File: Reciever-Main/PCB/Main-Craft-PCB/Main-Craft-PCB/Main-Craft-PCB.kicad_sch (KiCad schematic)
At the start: 17 parts

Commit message: Continue PCB work
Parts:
- added D? (x2): IR_Sender_?, symbol Device:LED
- added J? (x2): IR_Receiver_?, symbol Connector:Conn_01x03_Male
- added Q? (x2): 2N2219, Package_TO_SOT_THT:TO-39-3, symbol Transistor_BJT:2N2219
- added R? (x6): 10K, symbol Device:R
- added R? (x2): 4K7, symbol Device:R
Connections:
- net +5V: now also D?.2 (A), D?.2 (A), J?.3 (Pin_3), J?.3 (Pin_3), R?.1, R?.1
- net GND: now also J?.1 (Pin_1), J?.1 (Pin_1), Q?.1 (E), Q?.1 (E)
- net at D?.1 (K): now also R?.1; no longer Q?.3 (C) (x2)
- net ESC_? renamed BUZZER
- new net: D?.1 (K), R?.1 (x2)
- new net: Q?.3 (C), R?.2 (x4)
- new net: J?.2 (Pin_2), R?.2 (x2)
- new net: Q?.2 (B), R?.2 (x2)
- new net IR_?_OUT: R?.1, R?.1
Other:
- moved on the sheet: D?, Q?, R?

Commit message: Add components to the Schematic
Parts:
- added C? (x5): 100nF, symbol Device:C
- added D? (x2): 1N5817, Diode_THT:D_DO-41_SOD81_P10.16mm_Horizontal, symbol Diode:1N5817
- added SW?: SW_SPDT, symbol Switch:SW_SPDT
- added U?: LM2940-5.0, symbol Regulator_Linear:LM1117-3.3
- added U?: LM2940-3.0, symbol Regulator_Linear:LM1117-3.3
- J?: value Conn_02x04_Odd_Even -> nRF24L01_Conn
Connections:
- net +5V: now also U?.18 (+5V), C?.2, U?.2 (VO)
- net Earth: now reaches J?.1 (Pin_1)
- net Earth: now also C?.1, C?.1, C?.1, C?.1, C?.1, D?.2 (A), D?.2 (A), U?.1 (GND), U?.1 (GND)
- net +3V3: now reaches J?.2 (Pin_2)
- net +3V3: now also U?.16 (+3V3), C?.2, C?.2, U?.2 (VO)
- net NRF_CE: now reaches J?.3 (Pin_3)
- net NRF_CSN: now reaches J?.4 (Pin_4)
- net NRF_SCK: now reaches J?.5 (Pin_5)
- net NRF_MOSI: now reaches J?.6 (Pin_6)
- net NRF_MISO: now reaches J?.7 (Pin_7)
- net NRF_IRQ: now reaches J?.8 (Pin_8)
- new net +BATT: SW?.1 (A)
- new net BAT_PWR: C?.2, C?.2, D?.1 (K), D?.1 (K), SW?.2 (B), U?.3 (VI), U?.3 (VI)
- no-connect marks 0 -> 8
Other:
- moved on the sheet: J?

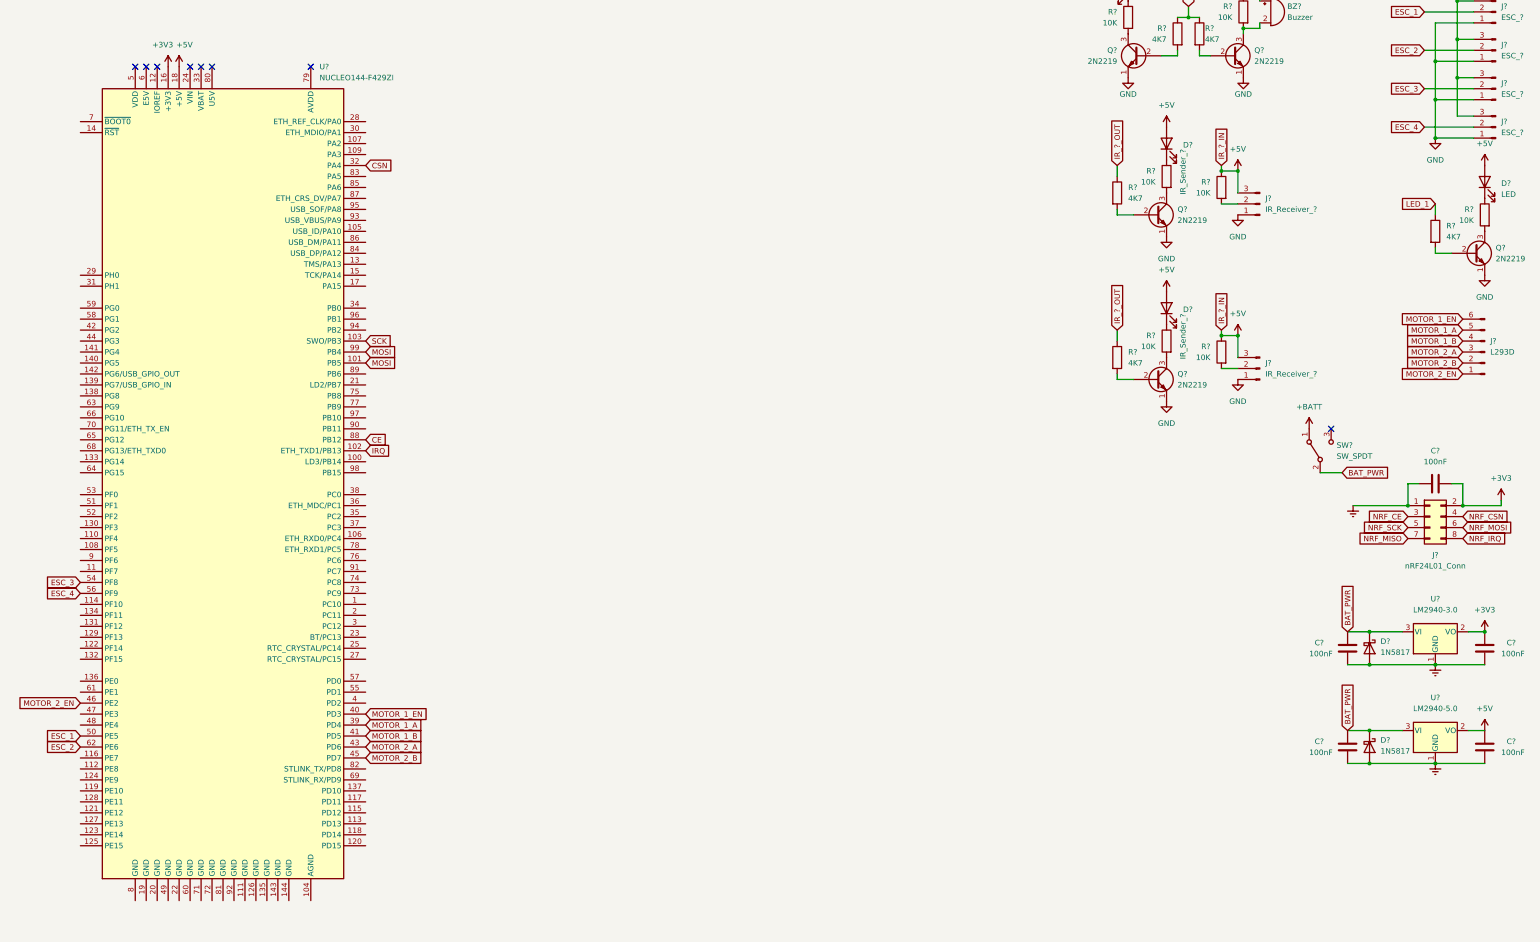
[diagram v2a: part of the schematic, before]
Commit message: Add Battery Comparitors to the Schematic
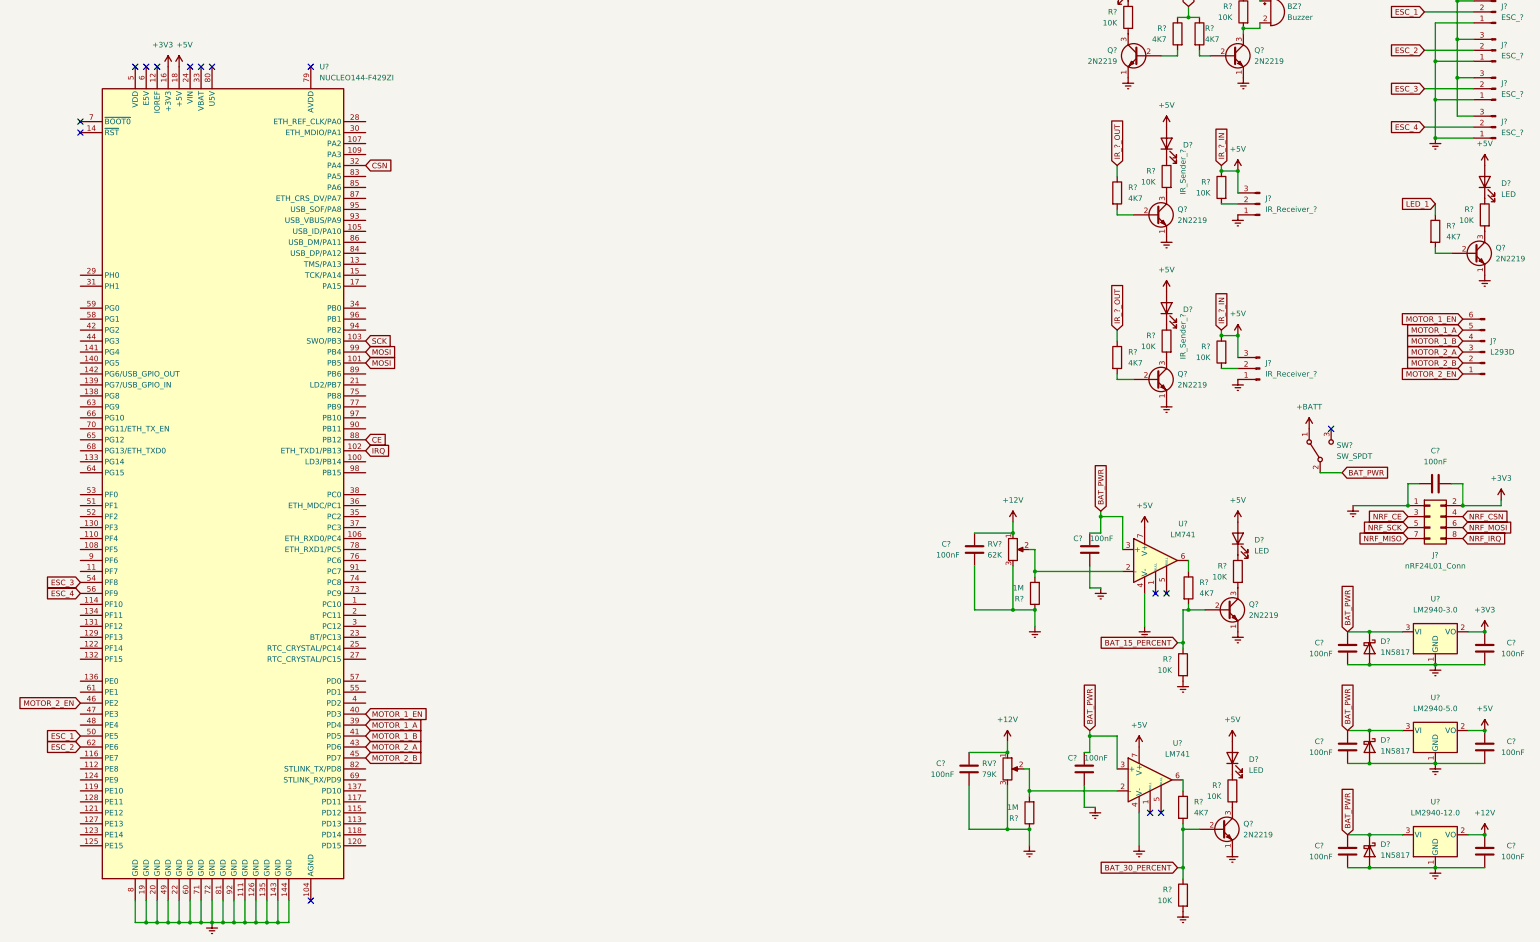
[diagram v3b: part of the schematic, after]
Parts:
- added C? (x4): 100nF, Capacitor_SMD:C_0603_1608Metric, symbol Device:C
- added C? (x2): 100nF, symbol Device:C
- added D? (x2): LED, symbol Device:LED
- added D?: 1N5817, Diode_THT:D_DO-41_SOD81_P10.16mm_Horizontal, symbol Diode:1N5817
- added Q? (x2): 2N2219, Package_TO_SOT_THT:TO-39-3, symbol Transistor_BJT:2N2219
- added R? (x2): 4K7, symbol Device:R
- added R? (x2): 1M, Resistor_SMD:R_0603_1608Metric, symbol Device:R
- added R? (x4): 10K, symbol Device:R
- added RV?: 79K, symbol Device:R_Potentiometer
- added RV?: 62K, symbol Device:R_Potentiometer
- added U? (x2): LM741, symbol Amplifier_Operational:LM741
- added U?: LM2940-12.0, symbol Regulator_Linear:LM1117-3.3
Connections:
- net GND is gone; now on net Earth: J?.1 (Pin_1), J?.1 (Pin_1), J?.1 (Pin_1), J?.1 (Pin_1), J?.1 (Pin_1), J?.1 (Pin_1), Q?.1 (E), Q?.1 (E), Q?.1 (E), Q?.1 (E), Q?.1 (E)
- net +5V: now also D?.2 (A), D?.2 (A), U?.7 (V+), U?.7 (V+)
- net BAT_PWR: now also C?.1, C?.1, C?.2, D?.1 (K), U?.3 (+), U?.3 (+), U?.3 (VI)
- net Earth: now also U?.111 (GND), U?.126 (GND), U?.135 (GND), U?.143 (GND), U?.144 (GND), U?.19 (GND), U?.20 (GND), U?.22 (GND), U?.49 (GND), U?.60 (GND), U?.71 (GND), U?.72 (GND), U?.8 (GND), U?.81 (GND), U?.92 (GND), C?.1, C?.1, C?.2, C?.2, C?.2, C?.2, D?.2 (A), Q?.1 (E), Q?.1 (E), R?.1, R?.1, R?.2, R?.2, RV?.3, RV?.3, U?.1 (GND), U?.4 (V-), U?.4 (V-)
- new net: R?.1, U?.6 (x2)
- new net: D?.1 (K), R?.1 (x2)
- new net: R?.2, RV?.2, U?.2 (-) (x2)
- new net: Q?.3 (C), R?.2 (x2)
- new net +12V: C?.1, C?.1, C?.2, RV?.1, RV?.1, U?.2 (VO)
- new net BAT_15_PERCENT: Q?.2 (B), R?.1, R?.2
- new net BAT_30_PERCENT: Q?.2 (B), R?.1, R?.2
- no-connect marks 8 -> 15

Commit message: Update PCB
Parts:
- added BT?: Battery, symbol Device:Battery
- added F?: Fuse, symbol Device:Fuse
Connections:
- net +BATT: now also C?.1, C?.1, C?.2, C?.2, C?.2, D?.1 (K), D?.1 (K), D?.1 (K), U?.3 (+), U?.3 (+), U?.3 (VI), U?.3 (VI), U?.3 (VI)
- net Earth: now also BT?.2 (-)
- removed net BAT_PWR: C?.1, C?.1, C?.2, C?.2, C?.2, D?.1 (K), D?.1 (K), D?.1 (K), SW?.2 (B), U?.3 (+), U?.3 (+), U?.3 (VI), U?.3 (VI), U?.3 (VI)
- new net: F?.1, SW?.2 (B)
- new net: BT?.1 (+), F?.2
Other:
- moved on the sheet: SW?

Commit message: Change library names, update PCB to add IR sensors LEDs and Switches
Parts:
- removed D? (x2): IR_Sender_?, symbol Device:LED
- removed J? (x2): IR_Receiver_?, symbol Connector:Conn_01x03_Male
- removed Q? (x2): 2N2219, Package_TO_SOT_THT:TO-39-3, symbol Transistor_BJT:2N2219
- removed R? (x4): 10K, symbol Device:R
- removed R? (x2): 4K7, symbol Device:R
- added D? (x12): LED, symbol Device:LED
- added J? (x4): IR_SENSOR_?, symbol Connector:Conn_01x03_Male
- added Q? (x9): 2N2219, Package_TO_SOT_THT:TO-39-3, symbol Transistor_BJT:2N2219
- added R? (x9): 4K7, symbol Device:R
- added R? (x23): 10K, symbol Device:R
- added R? (x11): 1K, symbol Device:R
- added SW? (x4): SW_SPDT, symbol Switch:SW_SPDT
- added SW? (x5): SW_Push, symbol Switch:SW_Push
- J?: value L293D -> L298N
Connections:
- net +12V: now also D?.2 (A)
- net +3V3: now also D?.2 (A)
- net +5V: now also D?.2 (A), D?.2 (A), D?.2 (A), D?.2 (A), D?.2 (A), D?.2 (A), D?.2 (A), D?.2 (A), D?.2 (A), D?.2 (A), J?.3 (Pin_3), J?.3 (Pin_3), J?.3 (Pin_3), J?.3 (Pin_3), SW?.2, SW?.2, SW?.2, SW?.2, SW?.2, SW?.2 (B), SW?.2 (B), SW?.2 (B), SW?.2 (B)
- net Earth: now also J?.1 (Pin_1), J?.1 (Pin_1), J?.1 (Pin_1), J?.1 (Pin_1), Q?.1 (E), Q?.1 (E), Q?.1 (E), Q?.1 (E), Q?.1 (E), Q?.1 (E), Q?.1 (E), Q?.1 (E), Q?.1 (E), R?.2, R?.2, R?.2, R?.2, R?.2, R?.2, R?.2, R?.2, R?.2, R?.2, R?.2, R?.2, R?.2, R?.2
- new net: Q?.2 (B), R?.2 (x9)
- new net: D?.1 (K), R?.1 (x12)
- new net: Q?.3 (C), R?.2 (x9)
- new net: R?.1, R?.1, SW?.3 (C) (x4)
- new net: R?.1, R?.1, SW?.1 (x5)
- new net: R?.1, R?.1, SW?.1 (A) (x2)
- new net IR_1: J?.2 (Pin_2)
- new net IR_2: J?.2 (Pin_2)
- new net IR_3: J?.2 (Pin_2)
- new net IR_4: J?.2 (Pin_2)
- new net LED_10: R?.1
- new net LED_2: R?.1
- new net LED_3: R?.1
- new net LED_4: R?.1
- new net LED_5: R?.1
- new net LED_6: R?.1
- new net LED_7: R?.1
- new net LED_8: R?.1
- new net LED_9: R?.1
- new net SW_1: R?.2
- new net SW_10: R?.2
- new net SW_11: R?.2
- new net SW_12: R?.2
- new net SW_13: R?.2
- new net SW_2: R?.2
- new net SW_3: R?.2
- new net SW_4: R?.2
- new net SW_5: R?.2
- new net SW_6: R?.2
- new net SW_7: R?.2
- no-connect marks 15 -> 17
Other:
- moved on the sheet: BT?, BZ?, C?, D?, F?, J?, Q?, R?, RV?, SW?, U?

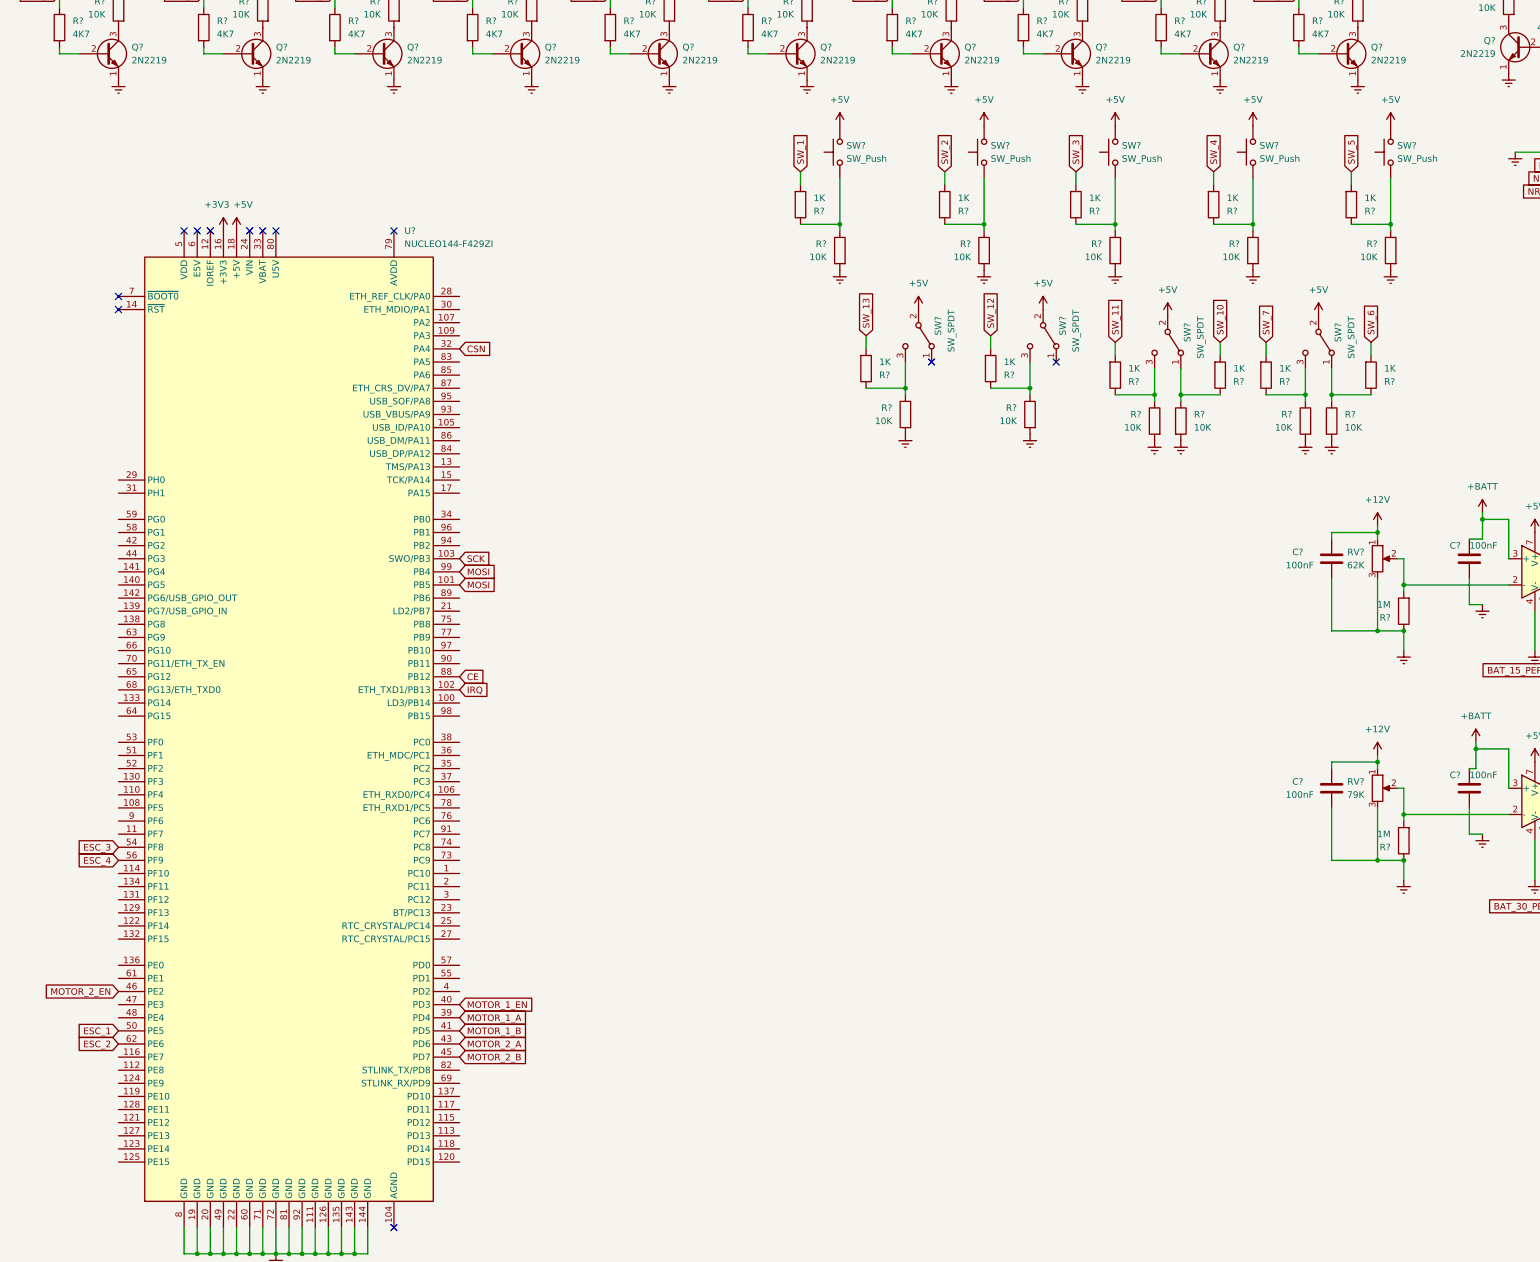
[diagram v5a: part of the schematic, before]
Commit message: Finish Pin mapping for PCB, update HARDWARE.h with updated pinmap
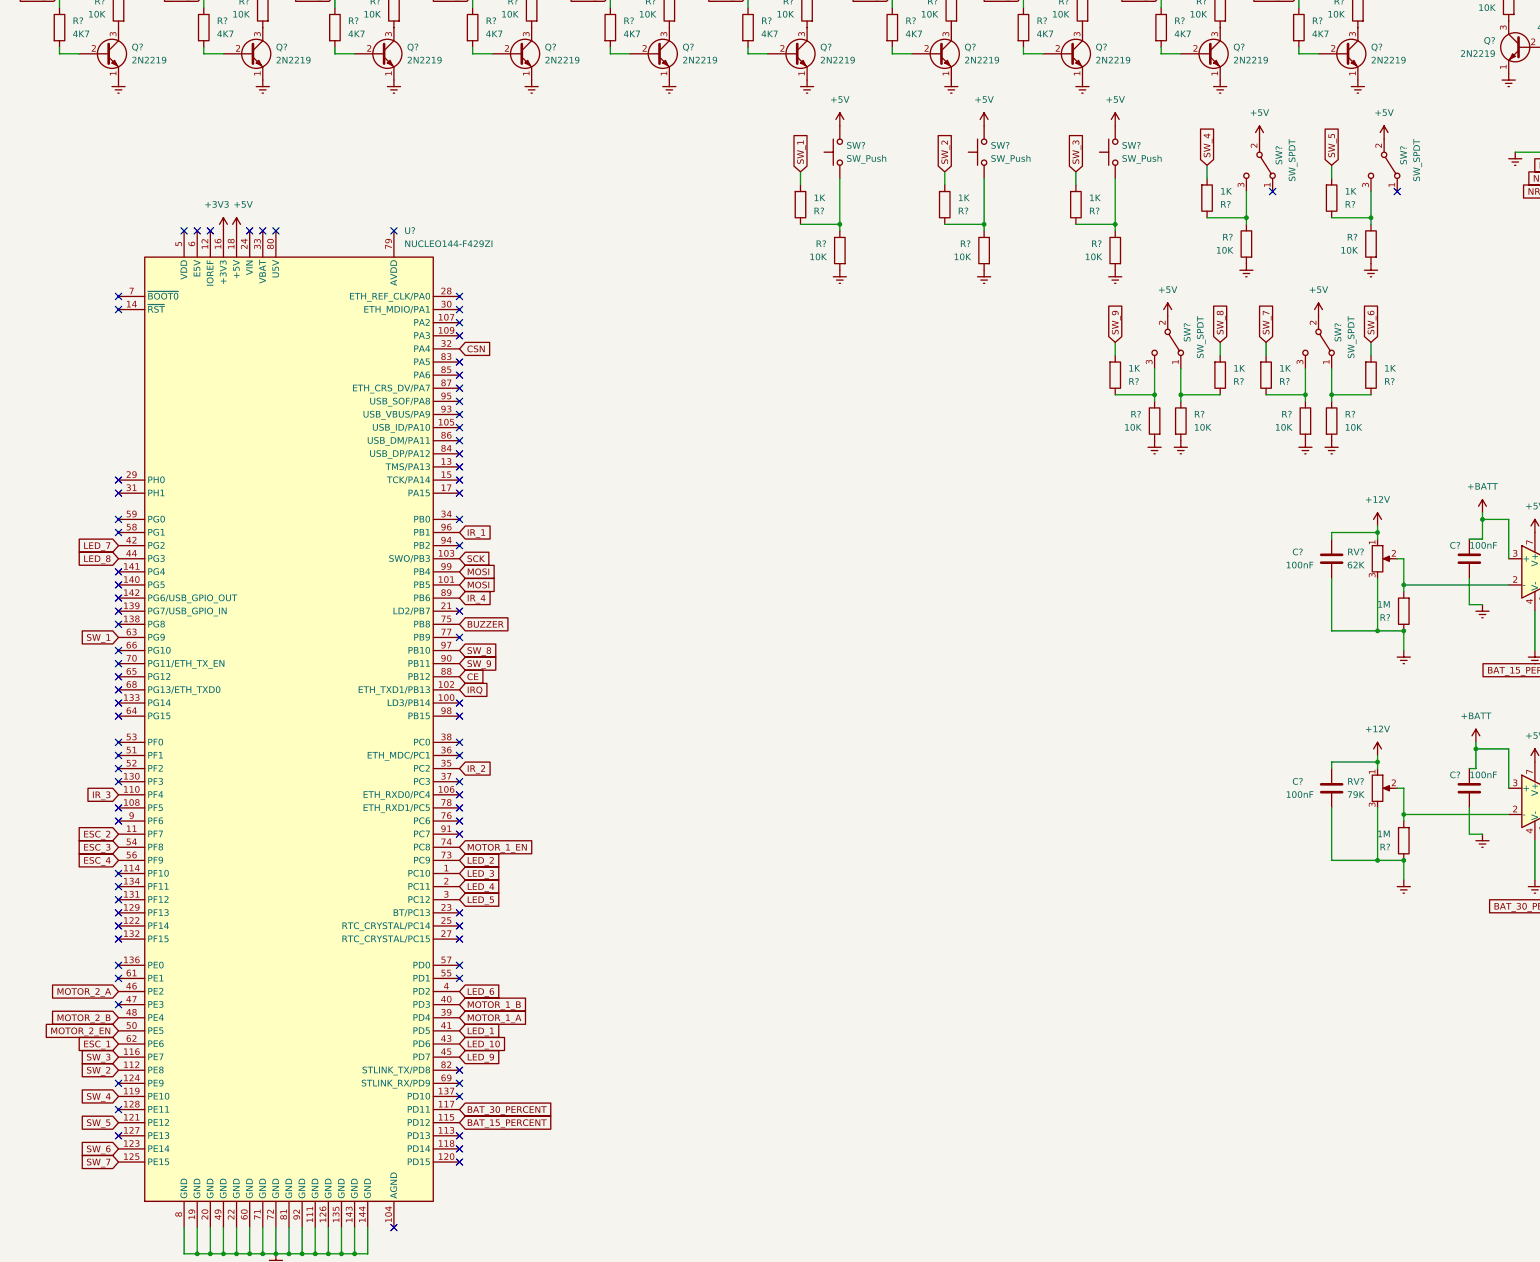
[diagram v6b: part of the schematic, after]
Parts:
- removed R? (x2): 10K, symbol Device:R
- removed R? (x2): 1K, symbol Device:R
- removed SW? (x2): SW_Push, symbol Switch:SW_Push
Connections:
- net SW_10 is gone; now on net SW_8: R?.2
- net SW_11 is gone; now on net SW_9: R?.2
- net SW_12 is gone; now on net SW_5: R?.2
- net SW_13 is gone; now on net SW_4: R?.2
- net BAT_15_PERCENT: now also U?.115 (PD12)
- net BAT_30_PERCENT: now also U?.117 (PD11)
- net BUZZER: now also U?.75 (PB8)
- net ESC_1: now also U?.62 (PE6); no longer U?.50 (PE5)
- net ESC_2: now also U?.11 (PF7); no longer U?.62 (PE6)
- net IR_1: now also U?.96 (PB1)
- net IR_2: now also U?.35 (PC2)
- net IR_3: now also U?.110 (PF4)
- net IR_4: now also U?.89 (PB6)
- net LED_1: now also U?.41 (PD5)
- net LED_10: now also U?.43 (PD6)
- net LED_2: now also U?.73 (PC9)
- net LED_3: now also U?.1 (PC10)
- net LED_4: now also U?.2 (PC11)
- net LED_5: now also U?.3 (PC12)
- net LED_6: now also U?.4 (PD2)
- net LED_7: now also U?.42 (PG2)
- net LED_8: now also U?.44 (PG3)
- net LED_9: now also U?.45 (PD7)
- net MOTOR_1_B: now also U?.40 (PD3); no longer U?.41 (PD5)
- net MOTOR_1_EN: now also U?.74 (PC8); no longer U?.40 (PD3)
- net MOTOR_2_A: now also U?.46 (PE2); no longer U?.43 (PD6)
- net MOTOR_2_B: now also U?.48 (PE4); no longer U?.45 (PD7)
- net MOTOR_2_EN: now also U?.50 (PE5); no longer U?.46 (PE2)
- net SW_1: now also U?.63 (PG9)
- net SW_2: now also U?.112 (PE8)
- net SW_3: now also U?.116 (PE7)
- net SW_4: now also U?.119 (PE10)
- net SW_5: now also U?.121 (PE12)
- net SW_6: now also U?.123 (PE14)
- net SW_7: now also U?.125 (PE15)
- net SW_9: now reaches U?.90 (PB11)
- net SW_8: now reaches U?.97 (PB10)
- no-connect marks 17 -> 89
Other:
- moved on the sheet: R?, SW?

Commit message: Update Footprints
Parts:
- BZ1: renamed from BZ?; footprint (none) -> My_library:Buzzer
- C10, C11, C5, C6, C7, C8, C9: renamed from C?; footprint (none) -> Capacitor_SMD:C_0603_1608Metric
- D1, D10, D11, D12, D13, D18, D19, D2, D3, D4, D5, D6, D7, D8, D9: renamed from D?; footprint (none) -> Diode_SMD:D_0603_1608Metric
- D14, D15, D16: renamed from D?; footprint Diode_THT:D_DO-41_SOD81_P10.16mm_Horizontal -> My_library:1N5817M
- D17: renamed from D?; footprint (none) -> My_library:1N5817M
- R1, R10, R11, R12, R13, R14, R15, R16, R17, R18, R19, R2, R20, R21, R22, R23, R24, R25, R26, R27, R28, R29, R3, R30, R31, R32, R33, R34, R35, R36, R37, R38, R4, R41, R42, R43, R44, R45, R46, R47, R48, R49, R5, R50, R51, R52, R53, R6, R7, R8, R9: renamed from R?; footprint (none) -> Resistor_SMD:R_0603_1608Metric
- RV1, RV2: renamed from RV?; footprint (none) -> My_library:35WR100KLFTR
- U2, U3: renamed from U?; footprint (none) -> My_library:741C
- gave numbers to parts that had none: 44
